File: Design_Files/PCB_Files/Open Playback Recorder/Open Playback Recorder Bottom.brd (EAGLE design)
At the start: 100 x 50 mm, 16 parts, among them J2 SJ1-3535NG, J3 SJ1-3535NG

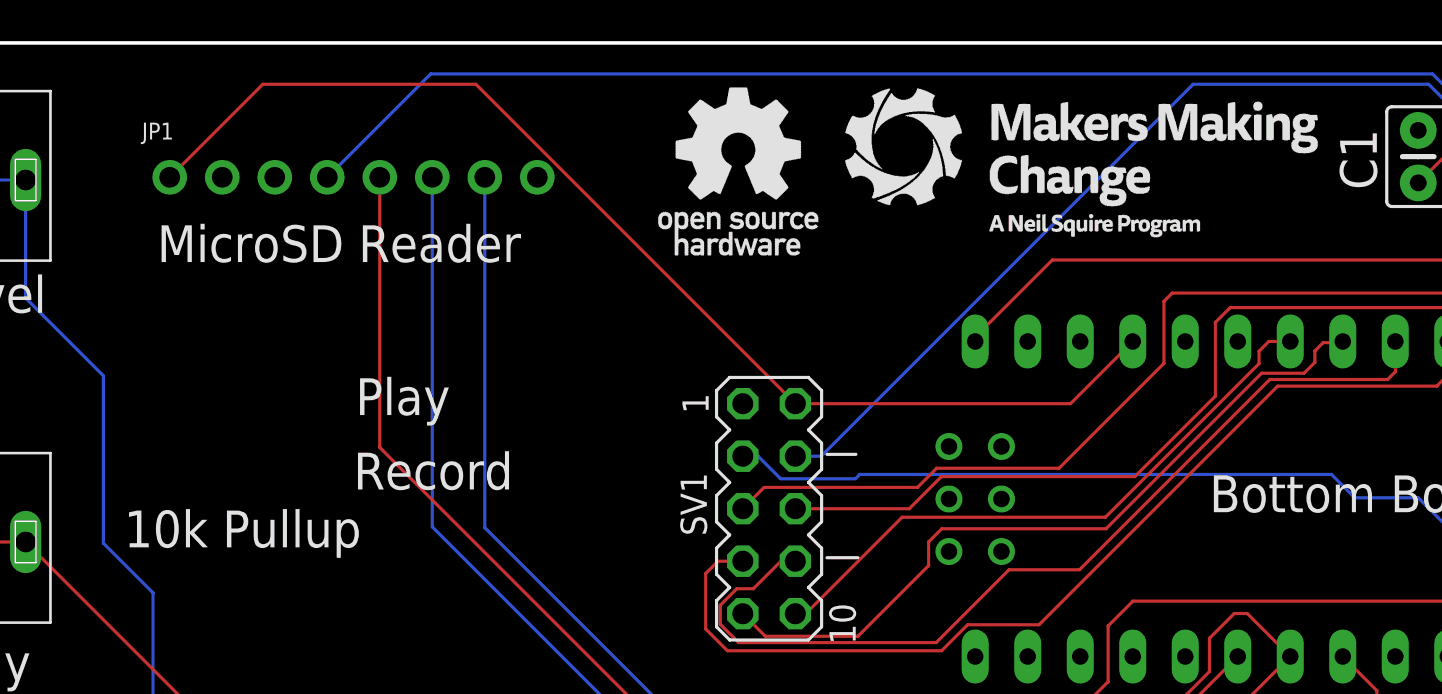
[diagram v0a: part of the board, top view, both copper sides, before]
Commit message: Updated files with OSHWA Certification
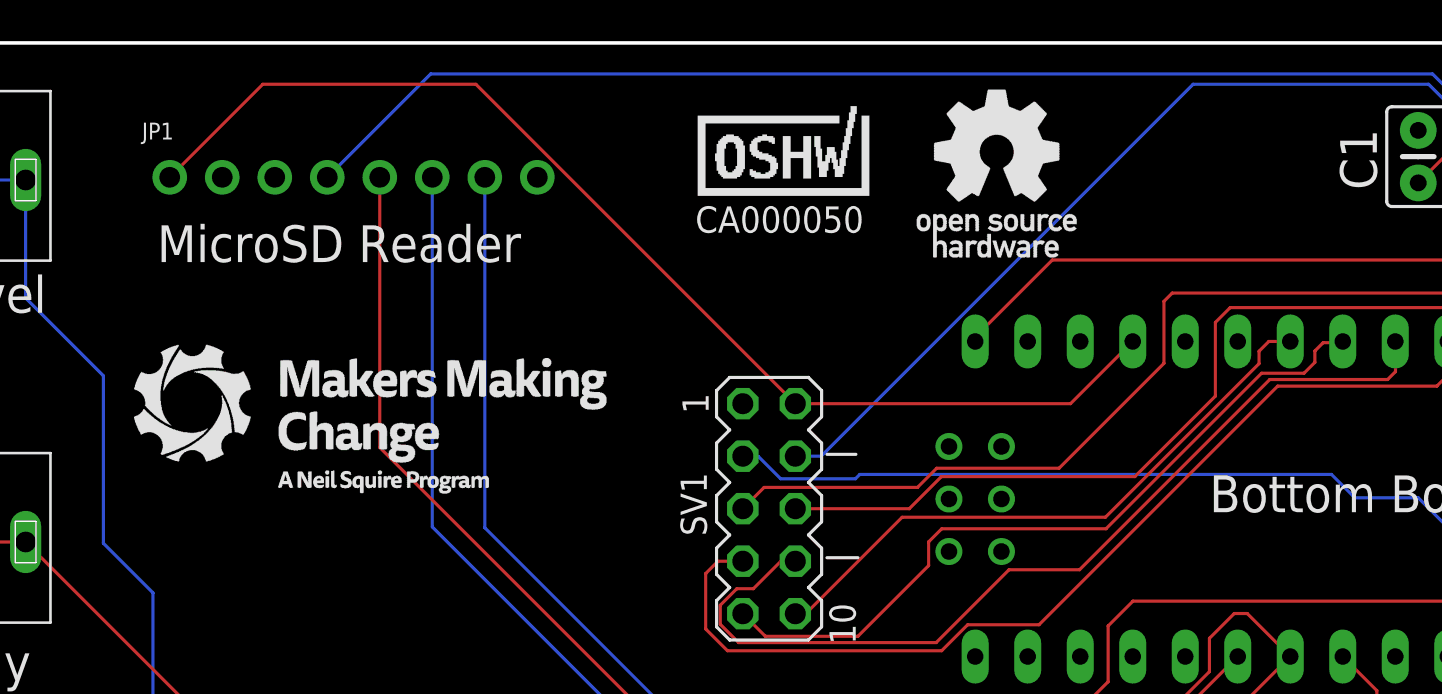
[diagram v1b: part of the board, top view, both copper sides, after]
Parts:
- added U$2: CA000050, MMC_Eagle:OSHWA-CERT-SMALL-SILK
- moved U$3 36.6 mm to (30.8, 31.8)
- moved U$4 12.5 mm to (61.2, 43.7)
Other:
- board text removed: "10k Pullup"
- board text removed: "Record"
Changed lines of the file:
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@@
 <wire x1="52.9" y1="30.1" x2="54.3" y2="30.1" width="0.1524" layer="21"/>
 <wire x1="52.9" y1="25.1" x2="54.4" y2="25.1" width="0.1524" layer="21"/>
-<text x="18.9" y="25.6" size="1.778" layer="21">10k Pullup</text>
-<text x="30.1" y="32" size="1.778" layer="21">Play</text>
-<text x="30" y="28.4" size="1.778" layer="21">Record</text>
 </plain>
 <attributes>
@@
 <element name="H1" library="MMC Eagle" library_urn="urn:adsk.eagle:library:13126479" package="HOLE-3MM-CLEAR" package3d_urn="urn:adsk.eagle:package:16268504/1" value="MOUNT-HOLE-3MM-CLEAR" x="5" y="5" smashed="yes"/>
 <element name="H3" library="MMC Eagle" library_urn="urn:adsk.eagle:library:13126479" package="HOLE-3MM-CLEAR" package3d_urn="urn:adsk.eagle:package:16268504/1" value="MOUNT-HOLE-3MM-CLEAR" x="95" y="30" smashed="yes"/>
-<element name="U$3" library="MMC_Eagle" library_urn="urn:adsk.eagle:library:44377252" package="MMC_MEDIUM_LOGO" package3d_urn="urn:adsk.eagle:package:44377670/1" value="" x="65.2" y="44.2" smashed="yes"/>
-<element name="U$4" library="MMC_Eagle" library_urn="urn:adsk.eagle:library:44377252" package="OSHW_SMALL_LOGO" package3d_urn="urn:adsk.eagle:package:44377674/1" value="" x="48.7" y="43.8" smashed="yes"/>
+<element name="U$3" library="MMC_Eagle" library_urn="urn:adsk.eagle:library:44377252" package="MMC_MEDIUM_LOGO" package3d_urn="urn:adsk.eagle:package:44377670/1" value="" x="30.8" y="31.8" smashed="yes"/>
+<element name="U$4" library="MMC_Eagle" library_urn="urn:adsk.eagle:library:44377252" package="OSHW_SMALL_LOGO" package3d_urn="urn:adsk.eagle:package:44377674/1" value="" x="61.2" y="43.7" smashed="yes"/>
+<element name="U$2" library="MMC_Eagle" library_urn="urn:adsk.eagle:library:44377252" package="OSHWA-CERT-SMALL-SILK" package3d_urn="urn:adsk.eagle:package:44378011/1" value="CA000050" x="50.8" y="42.6" smashed="yes">
+<attribute name="VALUE" x="46.53005625" y="40.822" size="1.27" layer="21" font="vector" ratio="12"/>
+</element>
 </elements>
 <signals>

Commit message: Minor changes to build files
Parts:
- moved S3 0.60 mm to (20.0, 6.10)
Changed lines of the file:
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@@
 </layers>
 <board>
-<fusionsync huburn="a.YnVzaW5lc3M6bmVpbHNxdWlyZQ" projecturn="a.YnVzaW5lc3M6bmVpbHNxdWlyZSMyMDIyMTIxMjU4ODQ4MDM4MQ" f3durn="urn:adsk.wipprod:dm.lineage:RpvBgM7aRKqYAMB9V_E1Dw" pcbguid="" lastpulledtime="2024-05-27T18:29:35Z" lastsyncedchangeguid="" latestrevisionid="6d18fd68-a1bb-43dc-acf0-3cef81a52a5e" lastsyncedrevisionid="6d18fd68-a1bb-43dc-acf0-3cef81a52a5e" lastboardhashguid="7ff0344c-72ac-49de-0f7e-615c607258a4" lastpushedtime="2024-06-17T17:31:42Z" linktopcb3d="true"/>
+<fusionsync huburn="a.YnVzaW5lc3M6bmVpbHNxdWlyZQ" projecturn="a.YnVzaW5lc3M6bmVpbHNxdWlyZSMyMDIyMTIxMjU4ODQ4MDM4MQ" f3durn="urn:adsk.wipprod:dm.lineage:RpvBgM7aRKqYAMB9V_E1Dw" pcbguid="" lastpulledtime="2024-05-27T18:29:35Z" lastsyncedchangeguid="" latestrevisionid="6d18fd68-a1bb-43dc-acf0-3cef81a52a5e" lastsyncedrevisionid="6d18fd68-a1bb-43dc-acf0-3cef81a52a5e" lastboardhashguid="7ff0344c-72ac-49de-0f7e-615c607258a4" lastpushedtime="2024-06-17T17:31:42Z" linktopcb3d="false"/>
 <plain>
 <text x="9.31" y="36.95" size="1.778" layer="25">Level</text>
@@
 <attribute name="VALUE" x="81.317" y="0.031" size="1.27" layer="27" ratio="10"/>
 </element>
-<element name="S3" library="MMC_Eagle" library_urn="urn:adsk.eagle:library:44377252" package="B3F-31XX" package3d_urn="urn:adsk.eagle:package:44377697/1" value="" x="20" y="5.5" smashed="yes">
-<attribute name="NAME" x="18.96" y="6.54" size="1.27" layer="25" ratio="10"/>
-<attribute name="VALUE" x="16.317" y="-0.469" size="1.27" layer="27" ratio="10"/>
+<element name="S3" library="MMC_Eagle" library_urn="urn:adsk.eagle:library:44377252" package="B3F-31XX" package3d_urn="urn:adsk.eagle:package:44377697/1" value="" x="20" y="6.1" smashed="yes">
+<attribute name="NAME" x="18.96" y="7.14" size="1.27" layer="25" ratio="10"/>
+<attribute name="VALUE" x="16.317" y="0.131" size="1.27" layer="27" ratio="10"/>
 </element>
 <element name="U$6" library="MMC_Eagle" library_urn="urn:adsk.eagle:library:44377252" package="SWITCH_SPDT_11MA1QS1" package3d_urn="urn:adsk.eagle:package:44377752/1" value="SWITCH-SPDT-OS102011" x="96.5" y="43.5" smashed="yes" rot="R90"/>
@@
 <contactref element="U$1" pad="D3"/>
 <contactref element="S3" pad="1"/>
-<wire x1="17.7394" y1="4.2554" x2="30.484" y2="17" width="0.1524" layer="1"/>
+<wire x1="17.7394" y1="4.8554" x2="29.884" y2="17" width="0.1524" layer="1"/>
 <wire x1="69.45" y1="17" x2="72.77" y2="20.32" width="0.1524" layer="1"/>
-<wire x1="30.484" y1="17" x2="69.45" y2="17" width="0.1524" layer="1"/>
+<wire x1="29.884" y1="17" x2="69.45" y2="17" width="0.1524" layer="1"/>
 <wire x1="6.9574" y1="42.30899375" x2="7.93299375" y2="41.3334" width="0.1524" layer="16"/>
 <wire x1="7.93299375" y1="41.3334" x2="9.84700625" y2="41.3334" width="0.1524" layer="16"/>
@@
 <wire x1="4.94" y1="45.37" x2="6.9574" y2="43.3526" width="0.1524" layer="16"/>
 <wire x1="9.84700625" y1="41.3334" x2="11.88360625" y2="43.37" width="0.1524" layer="16"/>
-<wire x1="17.7394" y1="4.2554" x2="18.4184" y2="4.2554" width="0.1524" layer="16"/>
-<wire x1="18.4184" y1="4.2554" x2="20.34735" y2="6.18435" width="0.1524" layer="16"/>
+<wire x1="17.7394" y1="4.8554" x2="19.0184" y2="4.8554" width="0.1524" layer="16"/>
+<wire x1="19.0184" y1="4.8554" x2="20.34735" y2="6.18435" width="0.1524" layer="16"/>
 <wire x1="20.34735" y1="6.18435" x2="20.34735" y2="7.30485" width="0.1524" layer="16"/>
 <wire x1="20.34735" y1="7.30485" x2="20.3" y2="7.3522" width="0.1524" layer="16"/>
